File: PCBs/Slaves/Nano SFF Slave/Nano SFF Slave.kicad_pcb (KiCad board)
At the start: 2 copper layers, 56 x 50 mm, 65 parts, among them J1 Screw_Terminal_01x02, J10 AVR-ISP-6, J11 Conn_01x06_Female, J12 Screw_Terminal_01x02, J13 Screw_Terminal_01x02, J14 Screw_Terminal_01x02, J15 Screw_Terminal_01x02, J16 Screw_Terminal_01x02, J2 Screw_Terminal_01x02, J3 Screw_Terminal_01x02, J4 Screw_Terminal_01x02, J5 Screw_Terminal_01x02, J6 Screw_Terminal_01x02, J7 Screw_Terminal_01x02, J8 Screw_Terminal_01x02, J9 Screw_Terminal_01x02, SW1 SW_DIP_x02, SW2 SW_DIP_x02, SW3 SW_MEC_5E, U1 ATmega328P-AU, U10 TISP4240M3BJR-S, U2 MAX487ESA+T, U3 ULN2003A, U4 MAX487CPA+, U5 AMS1117-5.0, U6 HY15P03C2, U7 TBU-CA065-200-WH, U8 TBU-CA065-200-WH, U9 TISP4240M3BJR-S, Y1 Crystal_GND24

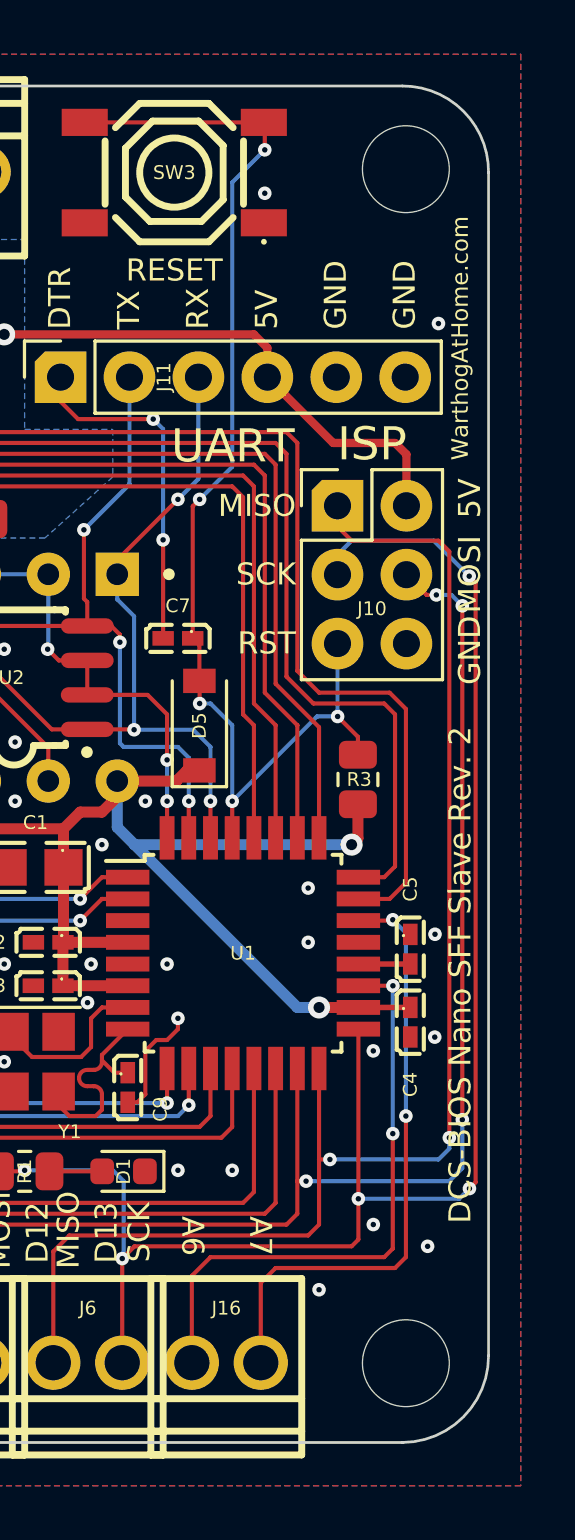
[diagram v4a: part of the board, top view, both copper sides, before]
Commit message: Fixed silkscreen on Nano SFF
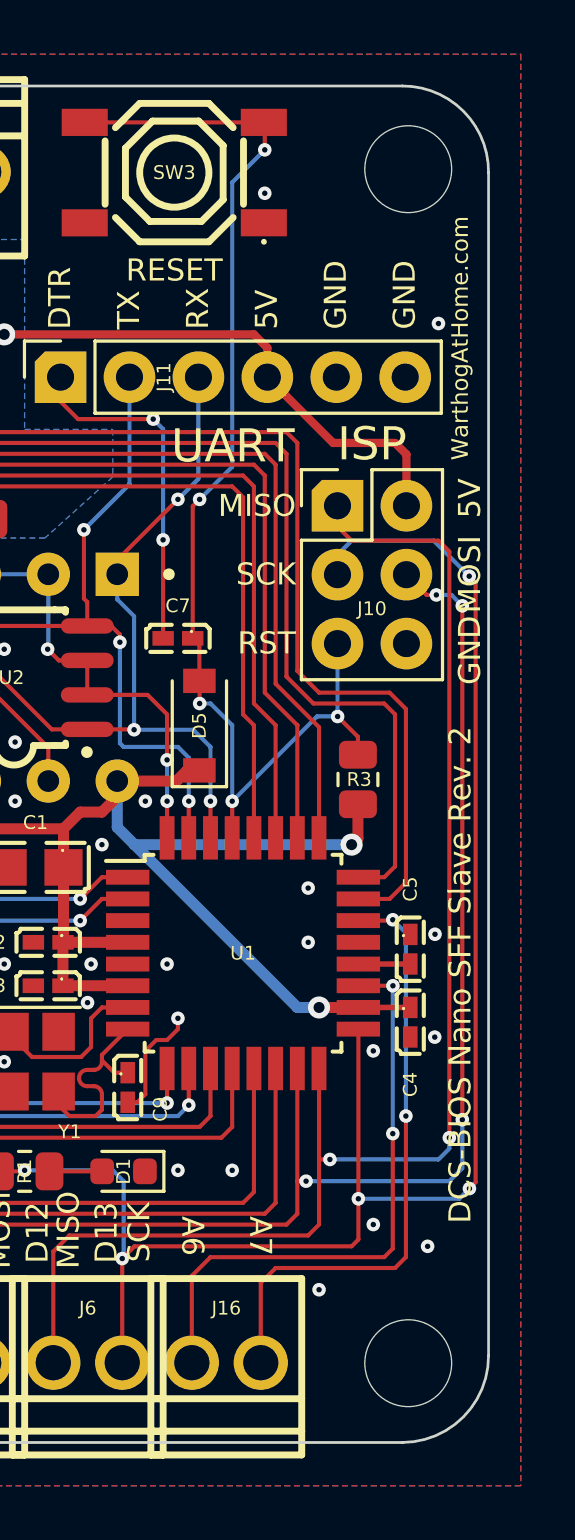
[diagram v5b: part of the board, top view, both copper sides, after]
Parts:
- moved H2 0.09 mm to (151.7, 83.0)
- moved H4 0.09 mm to (151.7, 127.0)
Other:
- board text added: "50MM →"
- board text removed: "47MM →"
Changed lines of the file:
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@@
   )
   (footprint "MountingHole:MountingHole_3.2mm_M3" (layer "F.Cu")
-    (at 151.62692 127)
+    (at 151.714 127)
     (descr "Mounting Hole 3.2mm, no annular, M3")
     (tags "mounting hole 3.2mm no annular m3")
@@
   )
   (footprint "MountingHole:MountingHole_3.2mm_M3" (layer "F.Cu")
-    (at 151.62692 83)
+    (at 151.714 83)
     (descr "Mounting Hole 3.2mm, no annular, M3")
     (tags "mounting hole 3.2mm no annular m3")
@@
     )
   )
+  (gr_circle (center 126.826982 104.890536) (end 151.826982 104.890536) (layer "B.SilkS") (width 0.127) (fill none))
   (gr_line (start 151.5 129.921) (end 101.873141 129.921) (layer "Edge.Cuts") (width 0.1))
   (gr_arc (start 101.873141 129.921) (mid 99.627211 128.981466) (end 98.698141 126.73116) (layer "Edge.Cuts") (width 0.1))
@@
     (effects (font (size 1.2192 1.2192) (thickness 0.1524)) (justify mirror))
   )
-  (gr_text "47MM →" (at 145.227242 83.087338) (layer "B.SilkS")
+  (gr_text "50MM →" (at 145.227242 83.087338) (layer "B.SilkS")
     (effects (font (size 1.2192 1.2192) (thickness 0.1524)) (justify mirror))
   )
@@
     (effects (font (size 1.2192 1.2192) (thickness 0.1524)) (justify mirror))
   )
-  (gr_text "BRRRRRRRRT" (at 128.425142 105.490138 15) (layer "B.SilkS")
+  (gr_text "BRRRRRRRRT" (at 126.826982 105.490138 15) (layer "B.SilkS")
     (effects (font (size 4.8768 4.8768) (thickness 0.6096)) (justify mirror))
   )

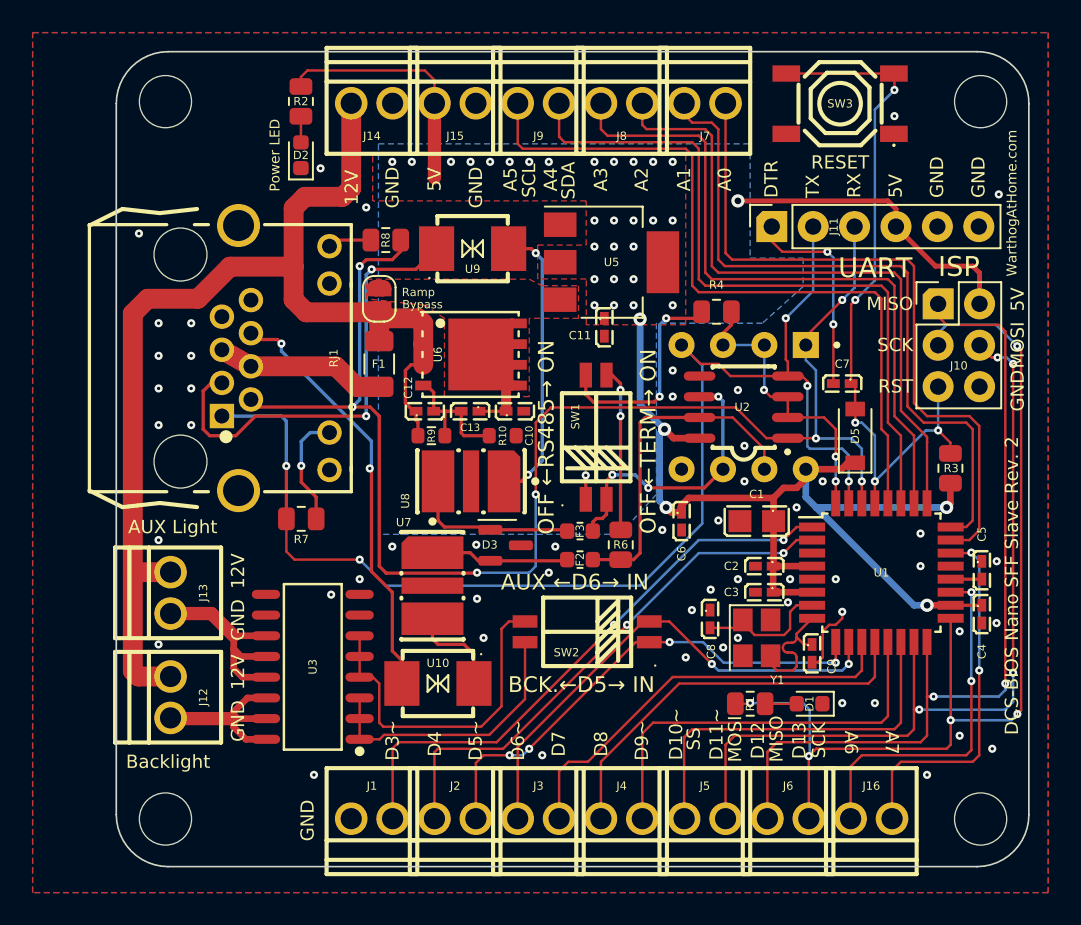
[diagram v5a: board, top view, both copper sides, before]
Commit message: Updated LCSC number and size of voltage ramp capacitors for Nano SFF Slave
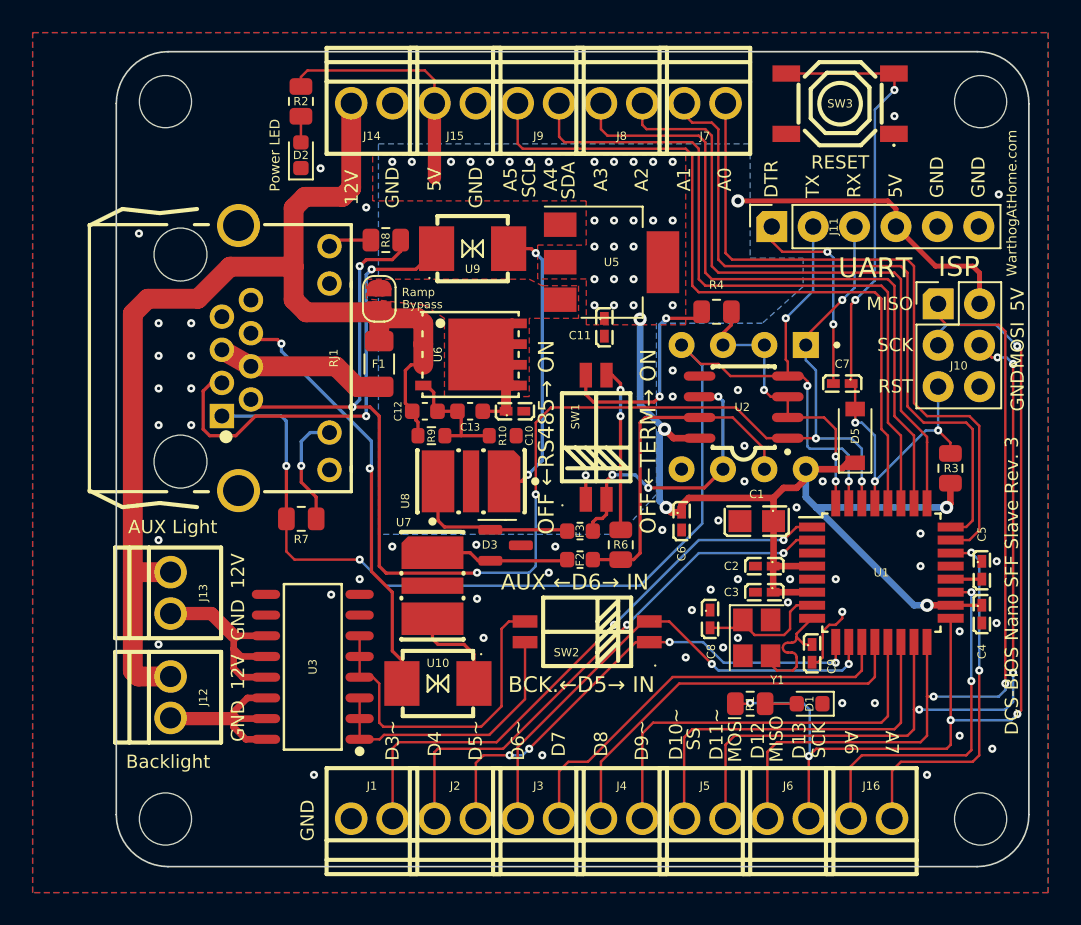
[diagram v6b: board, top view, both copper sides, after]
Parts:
- C12: value 500nF -> 470nF; footprint A10 KiCad Libraries:C0402 -> Capacitor_SMD:C_0603_1608Metric
- C13: value 50nF -> 47nF; footprint A10 KiCad Libraries:C0402 -> Capacitor_SMD:C_0603_1608Metric
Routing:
- net Net-(C12-Pad2): track 8.31 -> 7.42 mm

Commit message: Updated Nano SFF Slave for correct block terminal size
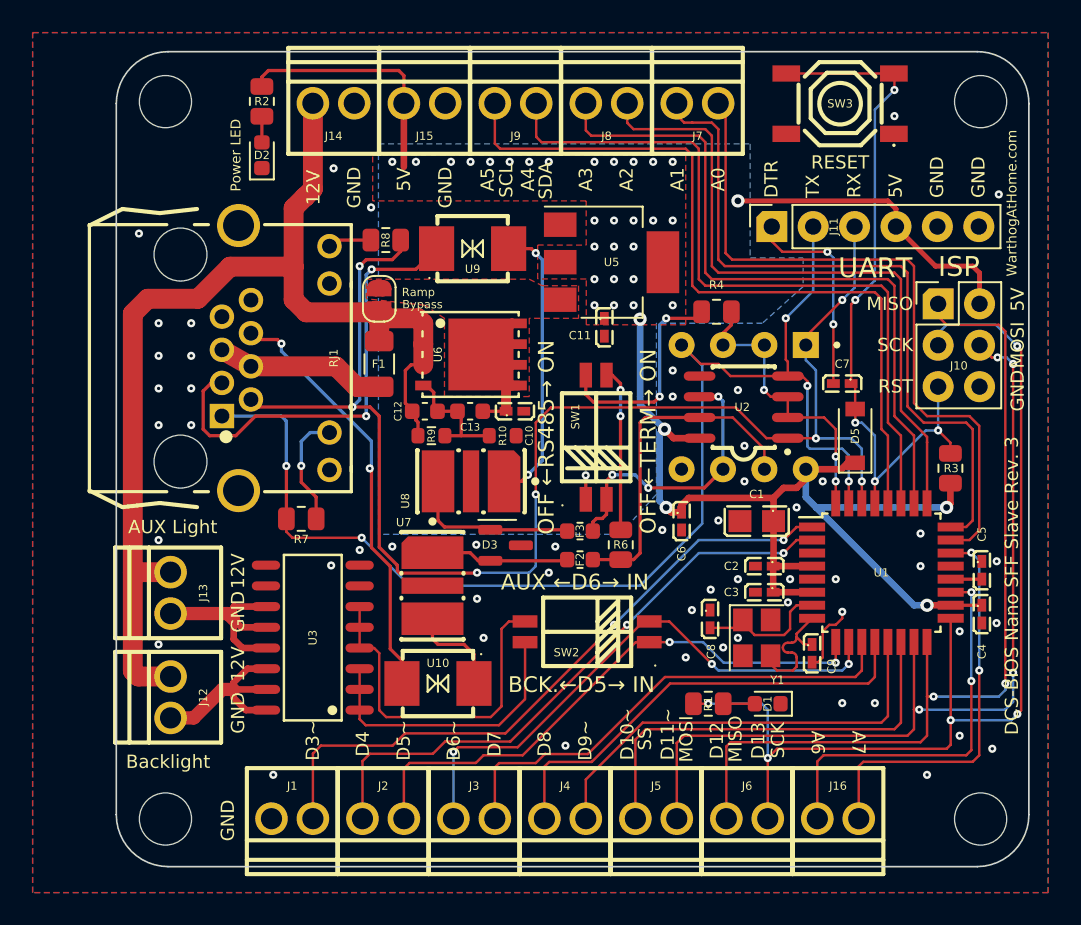
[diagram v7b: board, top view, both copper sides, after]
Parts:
- moved J1 4.89 mm to (109.5, 127.1)
- moved J2 4.42 mm to (115.1, 127.1)
- moved J3 3.94 mm to (120.6, 127.1)
- moved J4 3.47 mm to (126.2, 127.1)
- moved J5 2.99 mm to (131.8, 127.1)
- moved D1 2.57 mm to (138.7, 119.9)
- moved R1 2.57 mm to (135.0, 119.9)
- moved J6 2.52 mm to (137.4, 127.1)
- moved D2 2.40 mm to (107.6, 86.3)
- moved R2 2.40 mm to (107.6, 83.0)
- moved J14 2.35 mm to (112.0, 83.0)
- moved J16 2.04 mm to (143.0, 127.1)
- moved J15 1.88 mm to (117.6, 83.0)
- moved U3 1.79 mm to (110.8, 115.9)
- moved J9 1.40 mm to (123.2, 83.0)
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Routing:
- net D3: track 35.7 -> 40.4 mm
- net D5: track 30.4 -> 34.6 mm, vias 4 -> 2
- net D4: track 32.6 -> 36.7 mm
- net D7: track 25.8 -> 29.9 mm
- net D6: track 31.0 -> 34.8 mm, vias 2 -> 3
- net D8: track 24.6 -> 27.9 mm
- net D11: track 51.4 -> 54.4 mm
- net D10: track 23.6 -> 26.5 mm
- net D12: track 52.3 -> 55.0 mm
- net D13: track 61.5 -> 64.1 mm
- net 12V_Fused: track 71.3 -> 69.0 mm
- net A6: track 22.0 -> 24.2 mm
- net A7: track 22.6 -> 24.8 mm
- net D9: track 25.3 -> 27.1 mm
- net A4: track 44.1 -> 45.5 mm
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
